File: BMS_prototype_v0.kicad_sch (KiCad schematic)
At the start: 38 parts, among them J1 Conn_02x12_Odd_Even, J2 Conn_01x12_Pin

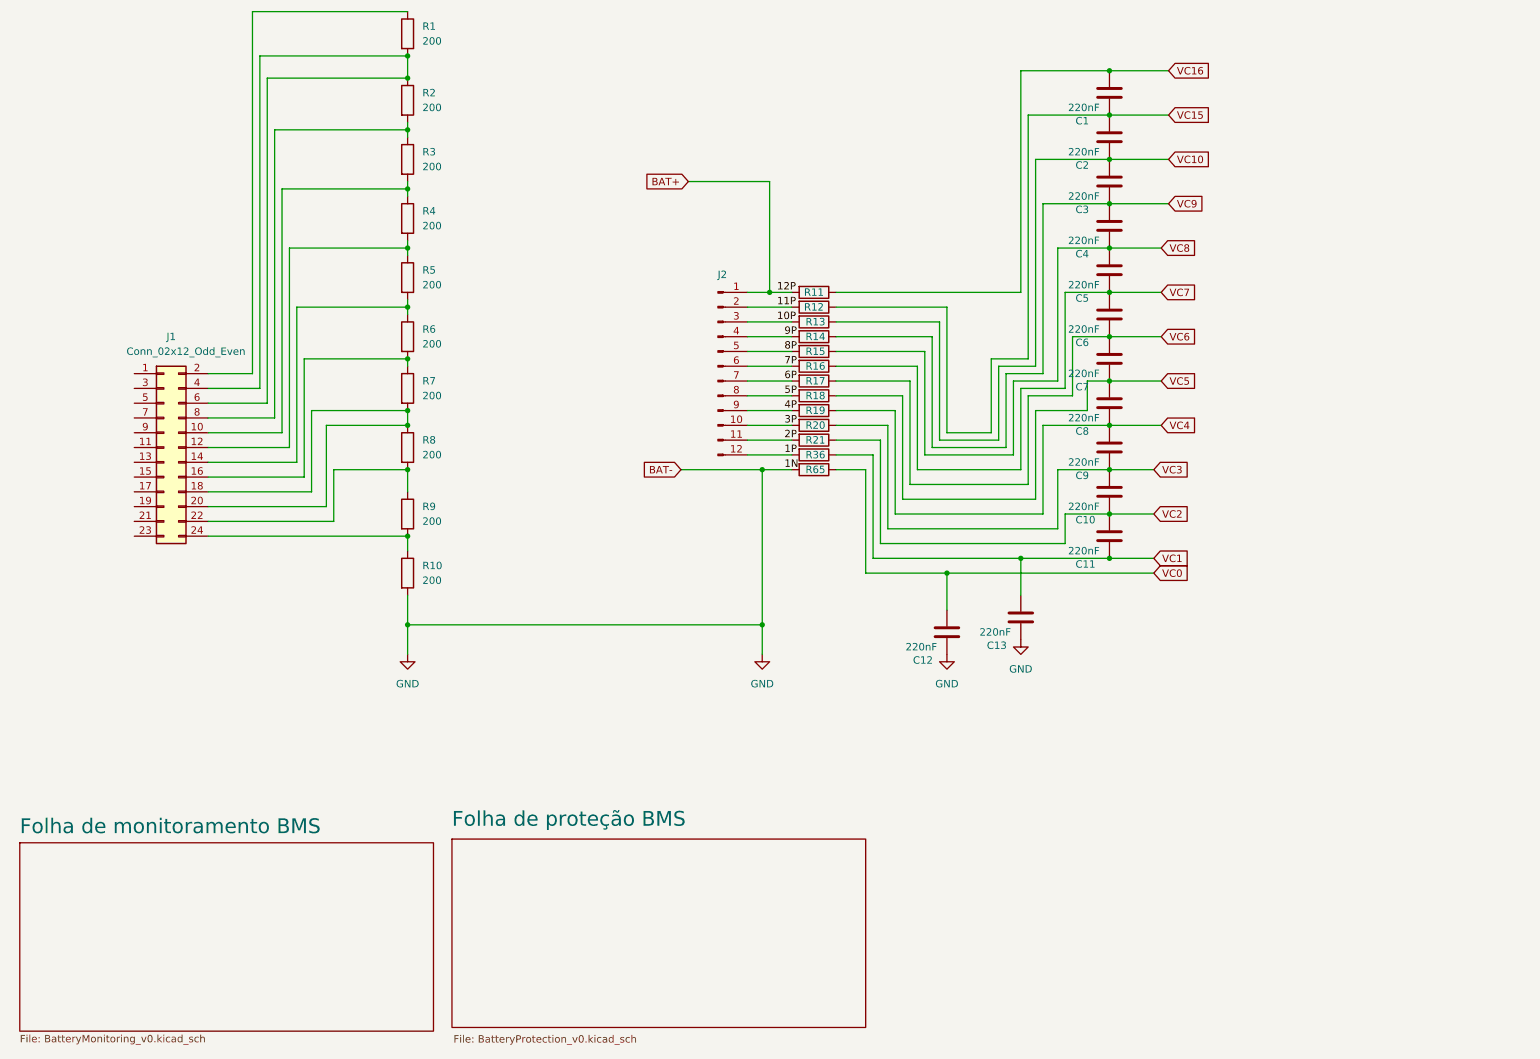
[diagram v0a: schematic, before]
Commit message: Inicio do roteamento e posicionamento da PCB
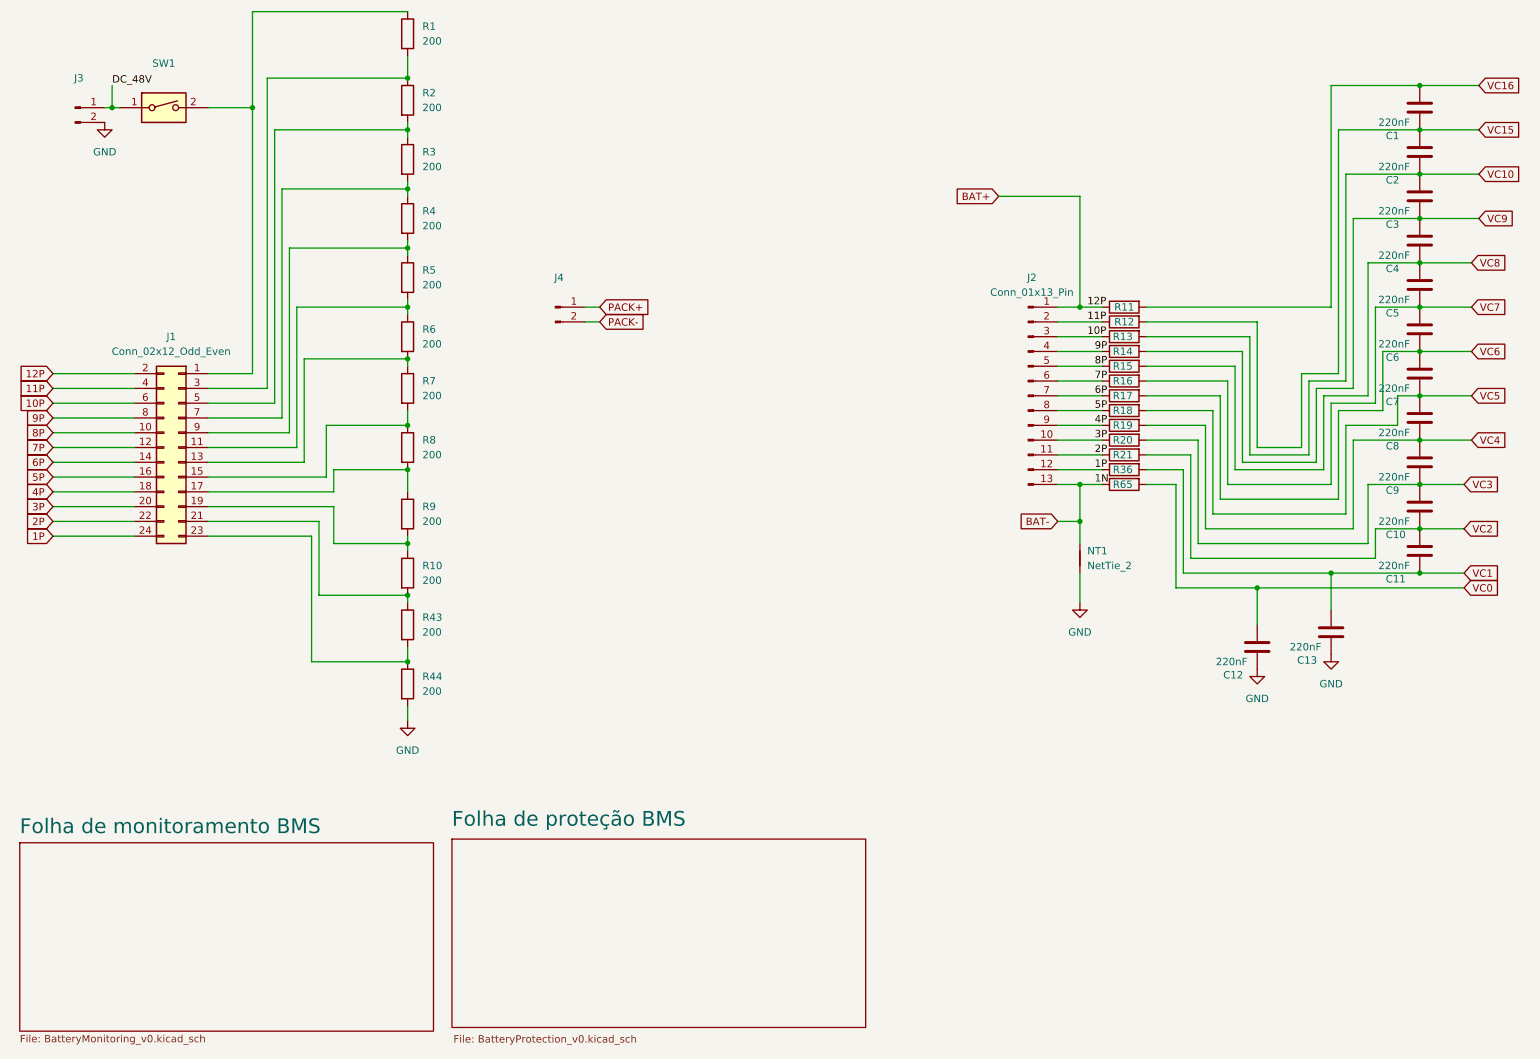
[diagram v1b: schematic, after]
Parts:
- removed J2: Conn_01x12_Pin, Connector_PinSocket_2.54mm:PinSocket_1x12_P2.54mm_Vertical, symbol Connector:Conn_01x12_Pin
- added J2: Conn_01x13_Pin, Connector_PinHeader_2.54mm:PinHeader_1x13_P2.54mm_Vertical, symbol Connector:Conn_01x13_Pin
- added J3, J4: Conn_01x02_Pin, Connector_PinHeader_2.54mm:PinHeader_1x02_P2.54mm_Vertical, symbol Connector:Conn_01x02_Pin
- added NT1: NetTie_2, NetTie:NetTie-2_SMD_Pad0.5mm, symbol Device:NetTie_2
- added R43, R44: 200, Resistor_SMD:R_1206_3216Metric, symbol Device:R
- added SW1: SW_DIP_x01, symbol Switch:SW_DIP_x01
- C1, C10, C11, C12, C13, C2, C3, C4, C5, C6, C7, C8, C9: footprint Capacitor_SMD:C_0402_1005Metric_Pad0.74x0.62mm_HandSolder -> Capacitor_SMD:C_1206_3216Metric_Pad1.33x1.80mm_HandSolder
- J1: footprint Connector_PinSocket_2.54mm:PinSocket_2x12_P2.54mm_Vertical -> Connector_PinHeader_2.54mm:PinHeader_2x12_P2.54mm_Vertical
- R1, R10, R2, R3, R4, R5, R6, R7, R8, R9: footprint (none) -> Resistor_SMD:R_1206_3216Metric
- R11, R12, R13, R14, R15, R16, R17, R18, R19, R20, R21, R36, R65: footprint Resistor_SMD:R_0402_1005Metric -> Resistor_SMD:R_1206_3216Metric
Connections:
- net BAT+ is gone; now on net VC16: R11.2
- net 10P: now also J1.6 (Pin_6), R13.1, J2.3 (Pin_3); no longer R13.2
- net 11P: now also J1.4 (Pin_4), R12.1, J2.2 (Pin_2); no longer R12.2
- net 1P: now also J1.24 (Pin_24), R36.1, J2.12 (Pin_12); no longer R36.2
- net 2P: now also J1.22 (Pin_22), R21.1, J2.11 (Pin_11); no longer R21.2
- net 3P: now also J1.20 (Pin_20), R20.1, J2.10 (Pin_10); no longer R20.2
- net 4P: now also J1.18 (Pin_18), R19.1, J2.9 (Pin_9); no longer R19.2
- net 5P: now also J1.16 (Pin_16), R18.1, J2.8 (Pin_8); no longer R18.2
- net 6P: now also J1.14 (Pin_14), R17.1, J2.7 (Pin_7); no longer R17.2
- net 7P: now also J1.12 (Pin_12), R16.1, J2.6 (Pin_6); no longer R16.2
- net 8P: now also J1.10 (Pin_10), R15.1, J2.5 (Pin_5); no longer R15.2
- net 9P: now also J1.8 (Pin_8), R14.1, J2.4 (Pin_4); no longer R14.2
- net GND: now also J3.2 (Pin_2), NT1.1, R44.2; no longer R10.2, R65.2
- net VC0: now also R65.2; no longer R65.1
- net VC1: now also R36.2; no longer R36.1
- net VC10: now also R13.2; no longer R13.1
- net VC15: now also R12.2; no longer R12.1
- net VC16: no longer R11.1
- net VC2: now also R21.2; no longer R21.1
- net VC3: now also R20.2; no longer R20.1
- net VC4: now also R19.2; no longer R19.1
- net VC5: now also R18.2; no longer R18.1
- net VC6: now also R17.2; no longer R17.1
- net VC7: now also R16.2; no longer R16.1
- net VC8: now also R15.2; no longer R15.1
- net VC9: now also R14.2; no longer R14.1
- net at R1.2, R2.1: now also J1.3 (Pin_3); no longer J1.4 (Pin_4), J1.6 (Pin_6)
- net at R2.2, R3.1: now also J1.5 (Pin_5); no longer J1.8 (Pin_8)
- net at R10.1, R9.2: now also J1.19 (Pin_19); no longer J1.24 (Pin_24)
- net at R4.2, R5.1: now also J1.9 (Pin_9); no longer J1.12 (Pin_12)
- net at R5.2, R6.1: now also J1.11 (Pin_11); no longer J1.14 (Pin_14)
- net at R8.2, R9.1: now also J1.17 (Pin_17); no longer J1.22 (Pin_22)
- net at J1.1 (Pin_1): now also R1.1, SW1.2
- net at R3.2, R4.1: now also J1.7 (Pin_7); no longer J1.10 (Pin_10)
- net at J1.13 (Pin_13): now also R6.2, R7.1
- net at J1.15 (Pin_15): now also R7.2, R8.1
- net 12P: now reaches J1.2 (Pin_2)
- net 12P: now also R11.1, J2.1 (Pin_1); no longer R1.1
- net at J1.21 (Pin_21): now also R10.2, R43.1
- net at J1.23 (Pin_23): now also R43.2, R44.1
- new net BAT-: J2.13 (Pin_13), NT1.2, R65.1
- new net DC_48V: J3.1 (Pin_1), SW1.1
- new net PACK+: J4.1 (Pin_1)
- new net PACK-: J4.2 (Pin_2)
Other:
- moved on the sheet: C1, C10, C11, C12, C13, C2, C3, C4, C5, C6, C7, C8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

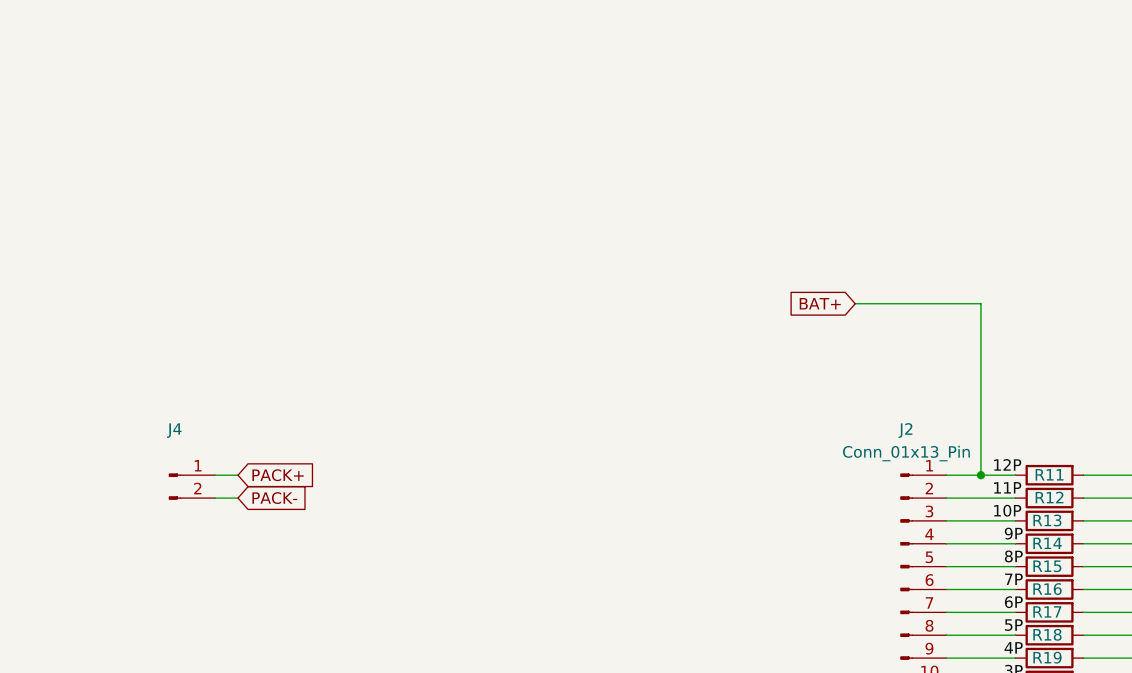
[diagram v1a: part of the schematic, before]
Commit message: add Res Shunt e atualiza para Kicad 9.0
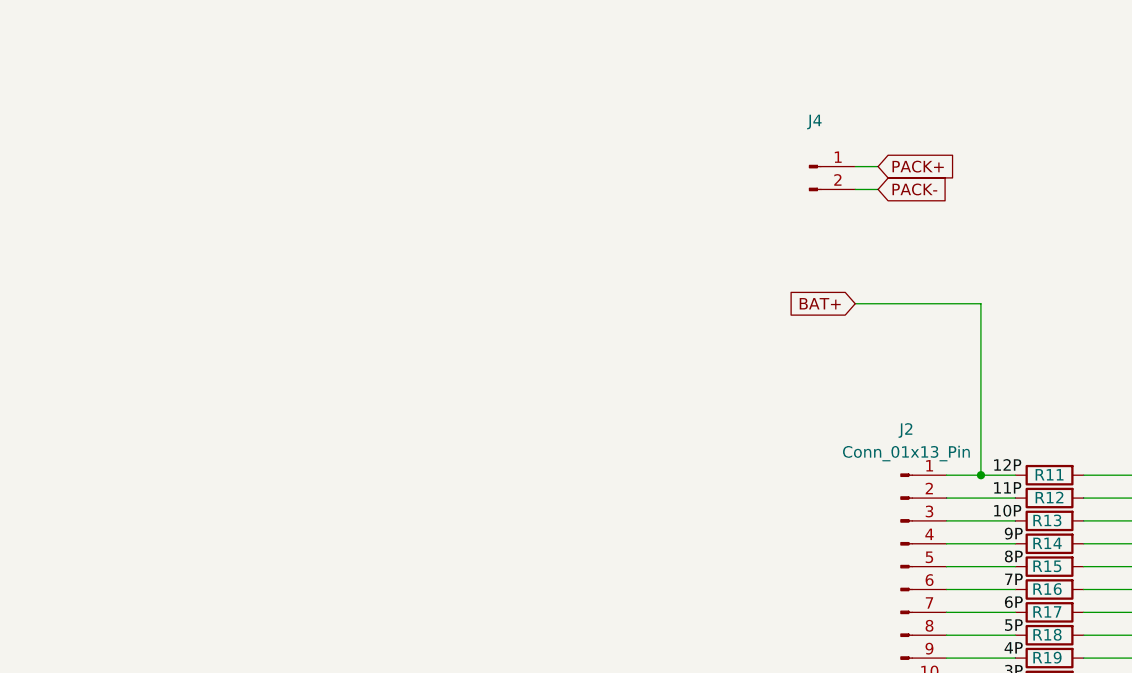
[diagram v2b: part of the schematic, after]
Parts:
- NT1: footprint NetTie:NetTie-2_SMD_Pad0.5mm -> NetTie:NetTie-2_SMD_Pad2.0mm
- SW1: footprint (none) -> Button_Switch_THT:SW_DIP_SPSTx01_Slide_6.7x4.1mm_W7.62mm_P2.54mm_LowProfile
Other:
- moved on the sheet: J4
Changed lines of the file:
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@@
 (kicad_sch
-	(version 20231120)
+	(version 20250114)
 	(generator "eeschema")
-	(generator_version "8.0")
+	(generator_version "9.0")
 	(paper "A4")
 	(title_block
@@
 	(wire
 		(pts
-			(xy 113.03 71.12) (xy 115.57 71.12)
+			(xy 184.15 36.83) (xy 186.69 36.83)
 		)
 		(stroke
@@
 	(wire
 		(pts
-			(xy 113.03 68.58) (xy 115.57 68.58)
+			(xy 184.15 34.29) (xy 186.69 34.29)
 		)
 		(stroke
@@
 	(label "12P"
 		(at 199.39 68.58 0)
-		(fields_autoplaced yes)
 		(effects
 			(font
@@
 	(label "5P"
 		(at 200.66 86.36 0)
-		(fields_autoplaced yes)
 		(effects
 			(font
@@
 	(label "3P"
 		(at 200.66 91.44 0)
-		(fields_autoplaced yes)
 		(effects
 			(font
@@
 	(label "11P"
 		(at 199.39 71.12 0)
-		(fields_autoplaced yes)
 		(effects
 			(font
@@
 	(label "1N"
 		(at 200.66 99.06 0)
-		(fields_autoplaced yes)
 		(effects
 			(font
@@
 	(label "DC_48V"
 		(at 31.75 30.48 0)
-		(fields_autoplaced yes)
 		(effects
 			(font
@@
 	(label "7P"
 		(at 200.66 81.28 0)
-		(fields_autoplaced yes)
 		(effects
 			(font
@@
 	(label "9P"
 		(at 200.66 76.2 0)
-		(fields_autoplaced yes)
 		(effects
 			(font
@@
 	(label "4P"
 		(at 200.66 88.9 0)
-		(fields_autoplaced yes)
 		(effects
 			(font
@@
 	(label "10P"
 		(at 199.39 73.66 0)
-		(fields_autoplaced yes)
 		(effects
 			(font
@@
 	(label "8P"
 		(at 200.66 78.74 0)
-		(fields_autoplaced yes)
 		(effects
 			(font
@@
 	(label "2P"
 		(at 200.66 93.98 0)
-		(fields_autoplaced yes)
 		(effects
 			(font
@@
 	(label "6P"
 		(at 200.66 83.82 0)
-		(fields_autoplaced yes)
 		(effects
 			(font
@@
 	(label "1P"
 		(at 200.66 96.52 0)
-		(fields_autoplaced yes)
 		(effects
 			(font
@@
 	(global_label "PACK+"
 		(shape input)
-		(at 115.57 68.58 0)
+		(at 186.69 34.29 0)
 		(fields_autoplaced yes)
 		(effects
@@
 		)
 		(property "Intersheetrefs" "${INTERSHEET_REFS}"
-			(at 125.0262 68.58 0)
+			(at 196.1462 34.29 0)
 			(effects
 				(font
@@
 	(global_label "PACK-"
 		(shape input)
-		(at 115.57 71.12 0)
+		(at 186.69 36.83 0)
 		(fields_autoplaced yes)
 		(effects
@@
 		)
 		(property "Intersheetrefs" "${INTERSHEET_REFS}"
-			(at 125.0262 71.12 0)
+			(at 196.1462 36.83 0)
 			(effects
 				(font
@@
 			)
 		)
-		(property "Footprint" "NetTie:NetTie-2_SMD_Pad0.5mm"
+		(property "Footprint" "NetTie:NetTie-2_SMD_Pad2.0mm"
 			(at 198.12 111.76 0)
 			(effects
@@
 			)
 		)
-		(property "Footprint" ""
+		(property "Footprint" "Button_Switch_THT:SW_DIP_SPSTx01_Slide_6.7x4.1mm_W7.62mm_P2.54mm_LowProfile"
 			(at 40.64 34.29 0)
 			(effects
@@
 	(symbol
 		(lib_id "Connector:Conn_01x02_Pin")
-		(at 107.95 68.58 0)
+		(at 179.07 34.29 0)
 		(unit 1)
 		(exclude_from_sim no)
@@
 		(fields_autoplaced yes)
 		(property "Reference" "J4"
-			(at 108.585 63.5 0)
+			(at 179.705 29.21 0)
 			(effects
 				(font
@@
 		)
 		(property "Value" "Conn_01x02_Pin"
-			(at 108.585 66.04 0)
+			(at 179.705 31.75 0)
 			(effects
 				(font
@@
 		)
 		(property "Footprint" "Connector_PinHeader_2.54mm:PinHeader_1x02_P2.54mm_Vertical"
-			(at 107.95 68.58 0)
+			(at 179.07 34.29 0)
 			(effects
 				(font
@@
 		)
 		(property "Datasheet" "~"
-			(at 107.95 68.58 0)
+			(at 179.07 34.29 0)
 			(effects
 				(font
@@
 		)
 		(property "Description" "Generic connector, single row, 01x02, script generated"
-			(at 107.95 68.58 0)
+			(at 179.07 34.29 0)
 			(effects
 				(font
@@
 		(at 90.17 160.02)
 		(size 71.12 32.385)
+		(exclude_from_sim no)
+		(in_bom yes)
+		(on_board yes)
+		(dnp no)
 		(stroke
 			(width 0.1524)
@@
 		(at 15.875 160.655)
 		(size 71.12 32.385)
+		(exclude_from_sim no)
+		(in_bom yes)
+		(on_board yes)
+		(dnp no)
 		(fields_autoplaced yes)
 		(stroke
@@
 		)
 	)
+	(embedded_fonts no)
 )

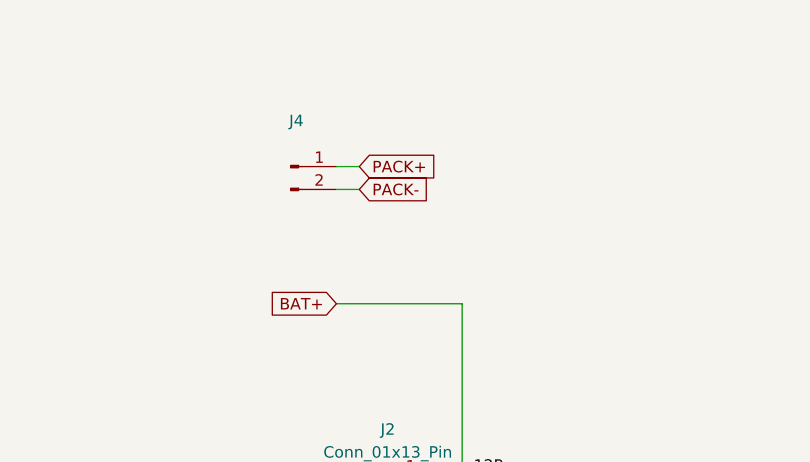
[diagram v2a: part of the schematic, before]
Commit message: Layout com footprints dos componentes da lista
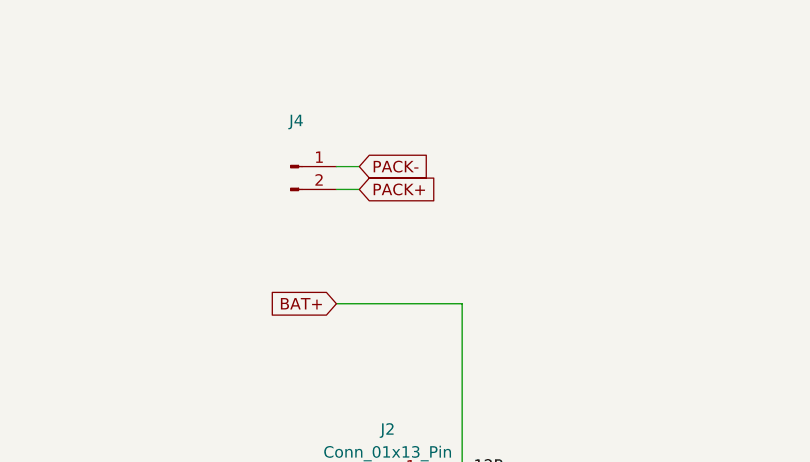
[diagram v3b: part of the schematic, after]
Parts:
- C1, C10, C11, C12, C13, C2, C3, C4, C5, C6, C7, C8, C9: Manufacturer_Part_Number (none) -> C1206C224J5RECAUTO
- J1: Manufacturer_Part_Number (none) -> G800W268018EU
- J2: Manufacturer_Part_Number (none) -> PH1-13-UA
- J3: Manufacturer_Part_Number (none) -> G800W306018EU
- J4: footprint Connector_PinHeader_2.54mm:PinHeader_1x02_P2.54mm_Vertical -> footprints:CONN_1935776_PXC; Manufacturer_Part_Number (none) -> G800W306018EU
- NT1: footprint NetTie:NetTie-2_SMD_Pad2.0mm -> NetTie:NetTie-2_SMD_Pad0.5mm
- R1, R10, R2, R3, R4, R43, R44, R5, R6, R7, R8, R9: Manufacturer_Part_Number (none) -> CR1206-FX-2000ELF
- R11, R12, R13, R14, R15, R16, R17, R18, R19, R20, R21, R36, R65: value R -> 20; Manufacturer_Part_Number (none) -> RC1206FR-0720RL
- SW1: footprint Button_Switch_THT:SW_DIP_SPSTx01_Slide_6.7x4.1mm_W7.62mm_P2.54mm_LowProfile -> footprints:SWT31AAA3S1; Manufacturer_Part_Number (none) -> SW-T3-1A-A-A3-S1
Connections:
- net PACK+: now also J4.2 (Pin_2); no longer J4.1 (Pin_1)
- net PACK-: now also J4.1 (Pin_1); no longer J4.2 (Pin_2)
